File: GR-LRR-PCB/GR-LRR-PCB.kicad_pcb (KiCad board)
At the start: 2 copper layers, 180 x 120 mm, 59 parts, among them IC1 TLV75533PDBVR, IC2 MC1413DR2G, J1 DF40HC3.5-80DS-0.4V51, J10 Limit Switch, J13 UT Sensor, J14 BATT VIN JUMPER, J16 Conn_01x30_Pin, J17 GND JUMPER, J2 DF40HC3.5-80DS-0.4V51, J3 +BATT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

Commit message: save
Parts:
- added R6: R, Resistor_SMD:R_1206_3216Metric_Pad1.30x1.75mm_HandSolder, F.Cu at (155.5, 154.5)
- added R7: R, Resistor_SMD:R_1206_3216Metric_Pad1.30x1.75mm_HandSolder, F.Cu at (151.0, 154.5)
- added R8: R, Resistor_SMD:R_1206_3216Metric_Pad1.30x1.75mm_HandSolder, F.Cu at (146.4, 154.5)
- moved J2 130.6 mm to (231.3, 94.2)
- moved J1 130.6 mm to (231.3, 137.3)
- moved J16 74.5 mm to (205.7, 161.3), turned to 180 degrees
- moved J9 30.8 mm to (155.5, 160.8), turned to -90 degrees
- moved J8 30.7 mm to (129.6, 151.8), turned to 180 degrees
- moved R10 27.9 mm to (191.0, 156.2)
- moved R11 27.9 mm to (196.1, 156.2)
- moved R13 27.9 mm to (181.2, 148.9)
- moved R14 27.9 mm to (181.2, 154.1)
- moved Q2 27.9 mm to (185.7, 154.3)
- moved J13 27.9 mm to (196.1, 160.8)
- moved R4 21.9 mm to (163.7, 156.2)
- moved R5 21.9 mm to (170.1, 156.2)
- moved J10 21.9 mm to (164.3, 160.8)
- moved StepperMotor2 21.9 mm to (125.9, 160.6), turned to -90 degrees
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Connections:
- IC2 pad 14: unconnected-(IC2-OUT_5-Pad14) -> Net-(IC2-OUT_5)
- IC2 pad 15: unconnected-(IC2-OUT_6-Pad15) -> Net-(IC2-OUT_6)
- IC2 pad 16: unconnected-(IC2-OUT_7-Pad16) -> Net-(IC2-OUT_7)
- IC2 pad 8: unconnected-(IC2-GND-Pad8) -> GND
- J9 pad 1: unconnected-(J9-Pin_1-Pad1) -> +24V
- J9 pad 2: unconnected-(J9-Pin_2-Pad2) -> Net-(J9-Pin_2)
- J9 pad 3: unconnected-(J9-Pin_3-Pad3) -> Net-(J9-Pin_3)
- J9 pad 4: unconnected-(J9-Pin_4-Pad4) -> Net-(J9-Pin_4)
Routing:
- net VM: track 0.00 -> 194.7 mm
- net +5V: track 2.54 -> 166.9 mm, vias 0 -> 1
- net +24V: track 0.00 -> 147.8 mm
- net GND: track 7.64 -> 115.5 mm, vias 0 -> 6
- net BATT_VIN: track 0.00 -> 93.4 mm
- net SPREAD1: track 0.00 -> 86.0 mm
- net MS2_1: track 0.00 -> 83.4 mm
- net EN1: track 0.00 -> 80.9 mm
- net MS1_1: track 0.00 -> 80.9 mm
- net PWM_0: track 121.1 -> 43.3 mm, vias 0 -> 1
- net ANALOG_A3: track 0.00 -> 73.2 mm, vias 0 -> 1
- net Net-(K1-COM): track 0.00 -> 71.4 mm
- net ANALOG_A2: track 0.00 -> 70.3 mm, vias 0 -> 1
- net ANALOG_A7: track 0.00 -> 66.7 mm
- net DIR1: track 123.6 -> 190.0 mm, vias 0 -> 1
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
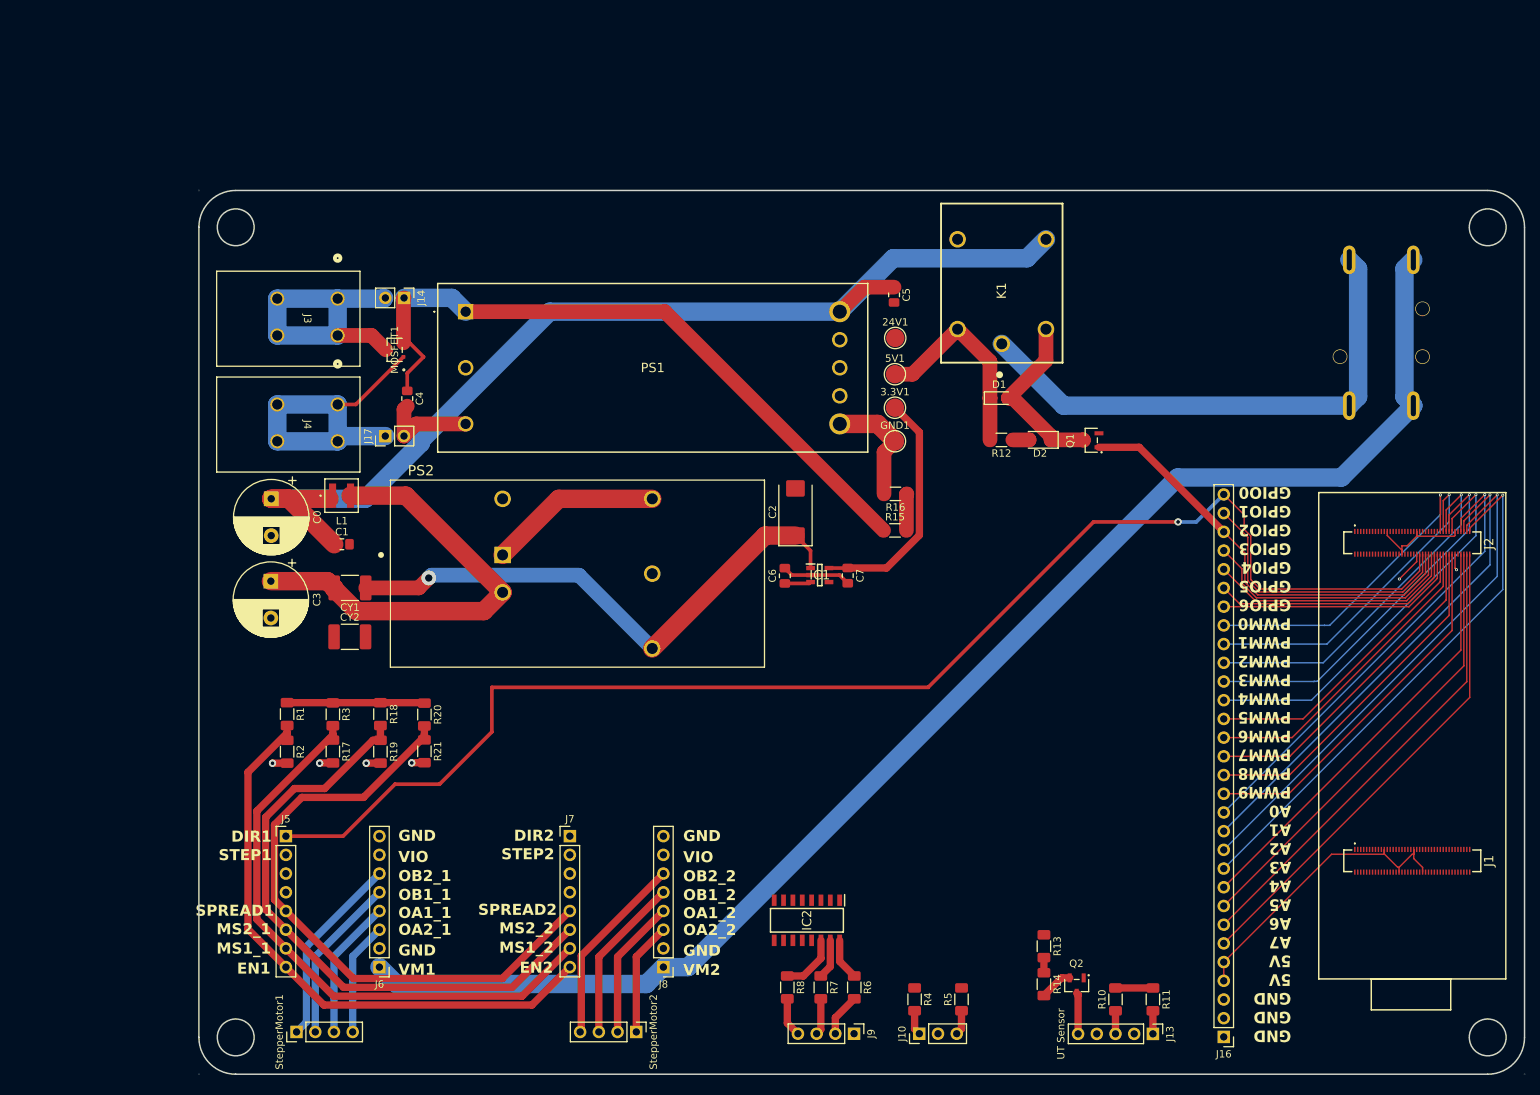
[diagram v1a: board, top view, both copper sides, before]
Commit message: new smaller layout
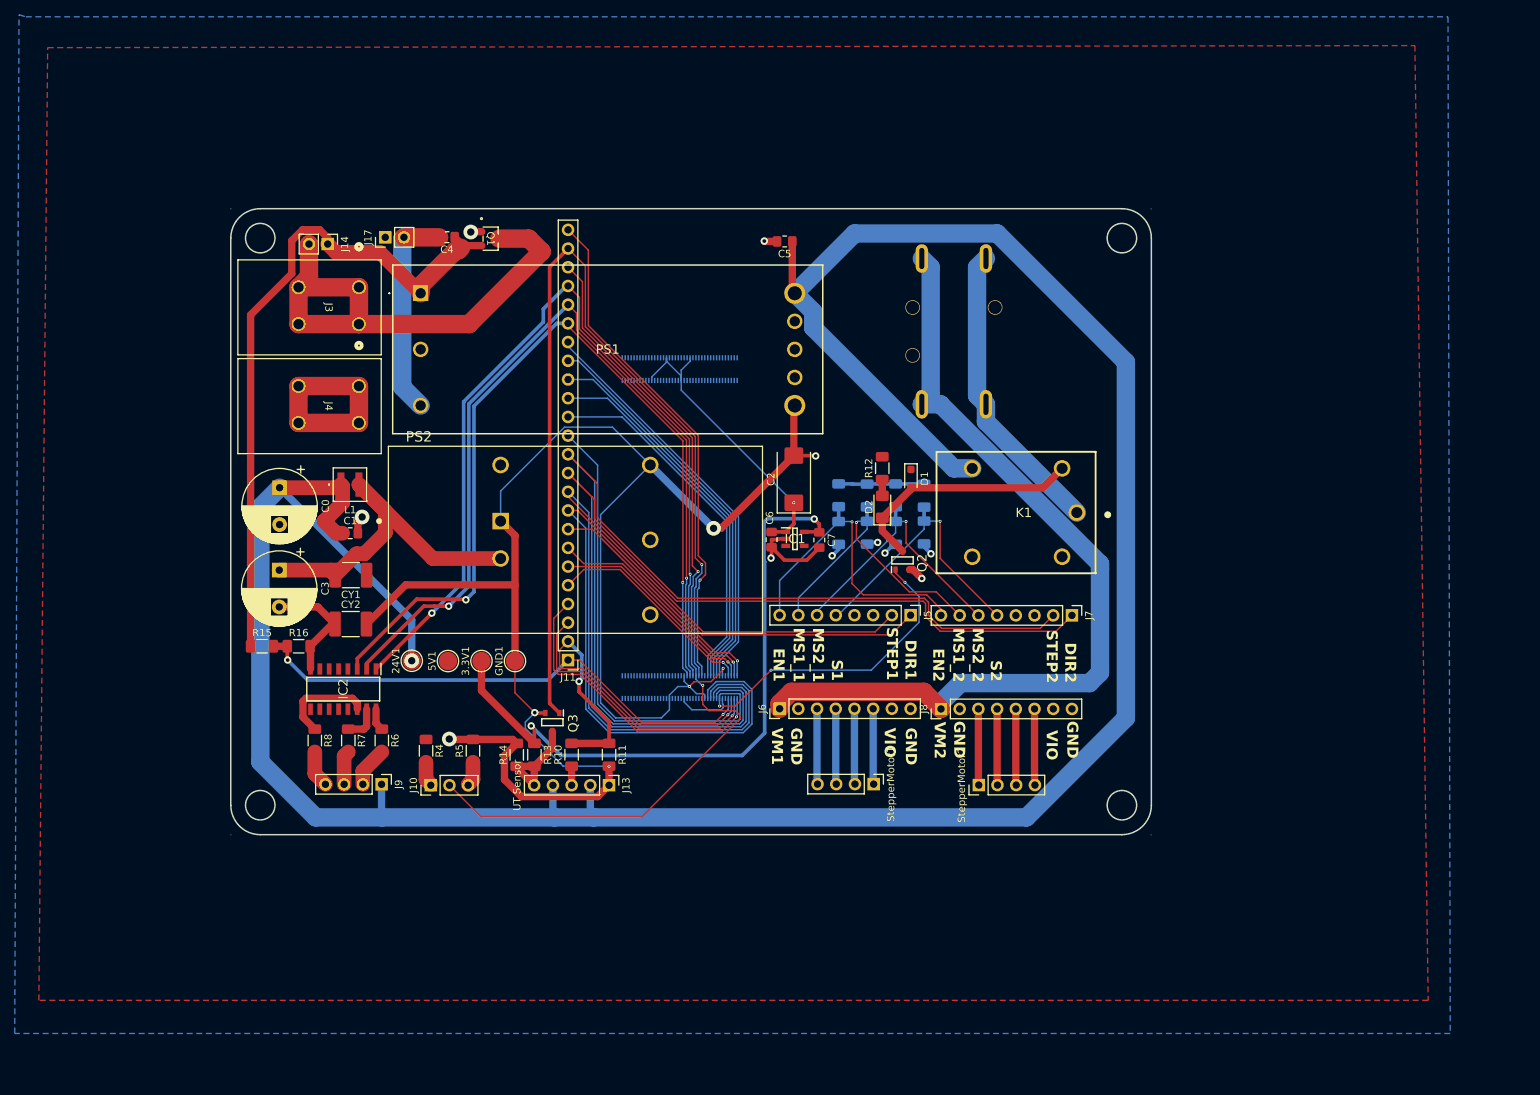
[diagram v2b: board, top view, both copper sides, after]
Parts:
- removed J16: Conn_01x30_Pin, Connector_PinHeader_2.54mm:PinHeader_1x30_P2.54mm_Vertical
- added J11: Conn_01x24_Pin, Connector_PinHeader_2.54mm:PinHeader_1x24_P2.54mm_Vertical, F.Cu at (116.6, 110.1)
- J1, J2: footprint DF40HC(3.5)-80DS-0.4V(51):DF40HC3580DS04V58 -> DF40HC3580DS04V58:DF40HC3580DS04V58; moved to B.Cu
- Q2: renamed from Q1; footprint BSS806NH6327XTSA1:BSS806NH6327XTSA1 -> BSS806NH6327XTSA1:SOT95P240X110-3N
- Q3: renamed from Q2; footprint BSS806NH6327XTSA1:BSS806NH6327XTSA1 -> BSS806NH6327XTSA1:SOT95P240X110-3N
- R1, R17, R18, R19, R2, R20, R21, R3: moved to B.Cu
- moved J1 119.8 mm to (131.8, 70.6)
- moved J2 101.4 mm to (131.8, 113.8)
- moved J5 90.0 mm to (163.1, 104.0), turned to -90 degrees
- moved R15 87.4 mm to (75.1, 108.2)
- moved StepperMotor1 85.3 mm to (158.1, 126.9), turned to -90 degrees
- moved R16 83.6 mm to (80.1, 108.2), turned to 0 degrees
- moved R2 82.6 mm to (153.4, 87.7), turned to 90 degrees
- moved J13 81.2 mm to (122.2, 127.1)
- moved R10 81.0 mm to (117.1, 122.9)
- moved R11 81.0 mm to (122.2, 122.9)
- moved R17 80.4 mm to (157.2, 87.7), turned to 90 degrees
- moved Q3 79.7 mm to (114.5, 118.5), turned to -90 degrees
- moved 24V1 78.9 mm to (95.4, 110.2), turned to 90 degrees
- moved R1 78.8 mm to (153.4, 92.8), turned to 90 degrees
- moved R19 78.1 mm to (161.1, 87.7), turned to 90 degrees
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- renumbered MOSFET1 to Q1
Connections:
- IC2 pad 1: unconnected-(IC2-IN_1-Pad1) -> 50_GPIO2_PD4
- IC2 pad 2: unconnected-(IC2-IN_2-Pad2) -> 48_GPIO1_PC15
- IC2 pad 3: unconnected-(IC2-IN_3-Pad3) -> 46_GPIO0_PC13
- J10 pad 2: GPIO_5 -> 52_GPIO3_PD5
- J2 pad 23: VCC -> unconnected-(J2-Pad23)
- J2 pad 33: unconnected-(J2-Pad33) -> GND
- J2 pad 34: VCC -> unconnected-(J2-Pad34)
- J2 pad 43: VCC -> unconnected-(J2-Pad43)
- J2 pad 46: DIR1 -> 46_GPIO0_PC13
- J2 pad 48: DIR2 -> 48_GPIO1_PC15
- J2 pad 50: GPIO_2 -> 50_GPIO2_PD4
- J2 pad 52: GPIO_3 -> 52_GPIO3_PD5
- J2 pad 54: GPIO_4 -> 54_GPIO4_PE3
- J2 pad 56: GPIO_5 -> 56_GPIO5_PG3
- J2 pad 57: unconnected-(J2-Pad57) -> GND
- J2 pad 58: GPIO_6 -> 58_GPIO6_PG10
- J2 pad 59: PWM_0 -> 59_PWM0_D6
- J2 pad 60: PWM_5 -> 60_PWM5_D1
- J2 pad 61: PWM_1 -> 61_PWM1_D5
- J2 pad 62: PWM_6 -> 62_PWM6_D0
- J2 pad 63: PWM_2 -> 63_PWM2_D4
- J2 pad 64: PWM_7 -> 64_PWM7_PJ7
- J2 pad 65: PWM_3 -> 65_PWM3_D3
- J2 pad 66: PWM_8 -> 66_PWM8_PJ10
- J2 pad 67: PWM_4 -> 67_PWM4_D2
- J2 pad 68: PWM_9 -> 68_PWM9_PH6
- J2 pad 69: VCC -> unconnected-(J2-Pad69)
- J2 pad 73: ANALOG_A0 -> 73_ANALOG_A0
- J2 pad 74: ANALOG_A4 -> 74_ANALOG_A4
- J2 pad 75: ANALOG_A1 -> 75_ANALOG_A1
- J2 pad 76: ANALOG_A5 -> 76_ANALOG_A5
- J2 pad 77: ANALOG_A2 -> 77_ANALOG_A2
- J2 pad 78: ANALOG_A6 -> 78_ANALOG_A6
- J2 pad 79: ANALOG_A3 -> 79_ANALOG_A3
- J2 pad 80: ANALOG_A7 -> 80_ANALOG_A7
- J5 pad 1: DIR1 -> 59_PWM0_D6
- J5 pad 2: PWM_0 -> 61_PWM1_D5
- J7 pad 1: DIR2 -> 63_PWM2_D4
- J7 pad 2: PWM_1 -> 65_PWM3_D3
- Q2 pad 1: GPIO_2 -> 67_PWM4_D2
- Q3 pad 1: GPIO_6 -> 54_GPIO4_PE3
- R10 pad 2: ANALOG_A0 -> 75_ANALOG_A1
- R11 pad 1: ANALOG_A0 -> 75_ANALOG_A1
- R15 pad 2: ANALOG_A1 -> 73_ANALOG_A0
- R16 pad 1: ANALOG_A1 -> 73_ANALOG_A0
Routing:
- net +24V: track 147.8 -> 373.1 mm, vias 0 -> 1
- net GND: track 115.5 -> 305.7 mm, vias 6 -> 12
- net DIR1: track 190.0 -> 0.00 mm, vias 1 -> 0
- net 63_PWM2_D4: track 0.00 -> 146.0 mm
- net 65_PWM3_D3: track 0.00 -> 145.4 mm
- net 54_GPIO4_PE3: track 0.00 -> 130.8 mm, vias 0 -> 1
- net 50_GPIO2_PD4: track 0.00 -> 123.1 mm, vias 0 -> 2
- net 52_GPIO3_PD5: track 0.00 -> 120.6 mm, vias 0 -> 2
- net 48_GPIO1_PC15: track 0.00 -> 120.1 mm, vias 0 -> 2
- net 59_PWM0_D6: track 0.00 -> 119.7 mm
- net +5V: track 166.9 -> 47.8 mm, vias 1 -> 5
- net 61_PWM1_D5: track 0.00 -> 118.3 mm
- net 46_GPIO0_PC13: track 0.00 -> 118.3 mm, vias 0 -> 2
- net 67_PWM4_D2: track 0.00 -> 106.6 mm, vias 0 -> 3
- net VM: track 194.7 -> 117.1 mm
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- added copper zone on F.Cu, net +5V
- added copper zone on B.Cu, net GND
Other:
- board size 180 x 120 mm -> 125 x 85 mm
- board text added: "A0 A1 A2 A3 A4 A5 A6 A7 PWM0_D6 PWM1_D5 PWM2_D4 PWM3_D3 PWM4_D2 PWM5_D1 PWM6_D0 PWM7_PJ7 PWM8_PJ10 PWM9_PH6 GPIO0_PC13 GPIO1_PC15 GPIO2_DP4 GPIO3_PD5 GPIO4_PE3 GPIO5_PG3"
- board text added: "GR-LRR 102523 A0"
- board text added: "S1"
- board text added: "S2"
- board text removed: "GND GND GND 5V 5V A7 A6 A5 A4 A3 A2 A1 A0 PWM9 PWM8 PWM7 PWM6 PWM5 PWM4 PWM3 PWM2 PWM1 PWM0 GPIO6 GPIO5 GPI04 GPIO3 GPIO2 GPIO1 GPIO0"
- board text removed: "OA1_1"
- board text removed: "OA1_2"
- board text removed: "OA2_1"
- board text removed: "OA2_2"
- board text removed: "OB1_1"
- board text removed: "OB1_2"
- board text removed: "OB2_1"
- board text removed: "OB2_2"
- board text removed: "SPREAD1"
- board text removed: "SPREAD2"

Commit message: new gerbers
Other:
- board text added: "GR-LRR 101523 A1"
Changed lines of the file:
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@@
     (effects (font (size 1.58 1.5) (thickness 0.3) bold) (justify left bottom mirror))
+  )
+  (gr_text "GR-LRR 101523 A1" (at 119.2276 52.9336) (layer "F.SilkS")
+    (effects (font (size 1.5 1.5) (thickness 0.3) bold) (justify left bottom))
   )
   (gr_text "DIR1" (at 162.2702 107.32 -90) (layer "F.SilkS")

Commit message: added step files
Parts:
- J11: moved to B.Cu
- turned J11 to 0 degrees
